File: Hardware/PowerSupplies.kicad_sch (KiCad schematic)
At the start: 56 parts, among them J3 Molex 26013114, J4 Molex 26013114, J5 Molex 26013114, J6 Molex 26013114, P1 XT60PW-M, U1 LM3414, U2 SY8303, U3 LM3414, U4 SY8303, U5 LM3414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

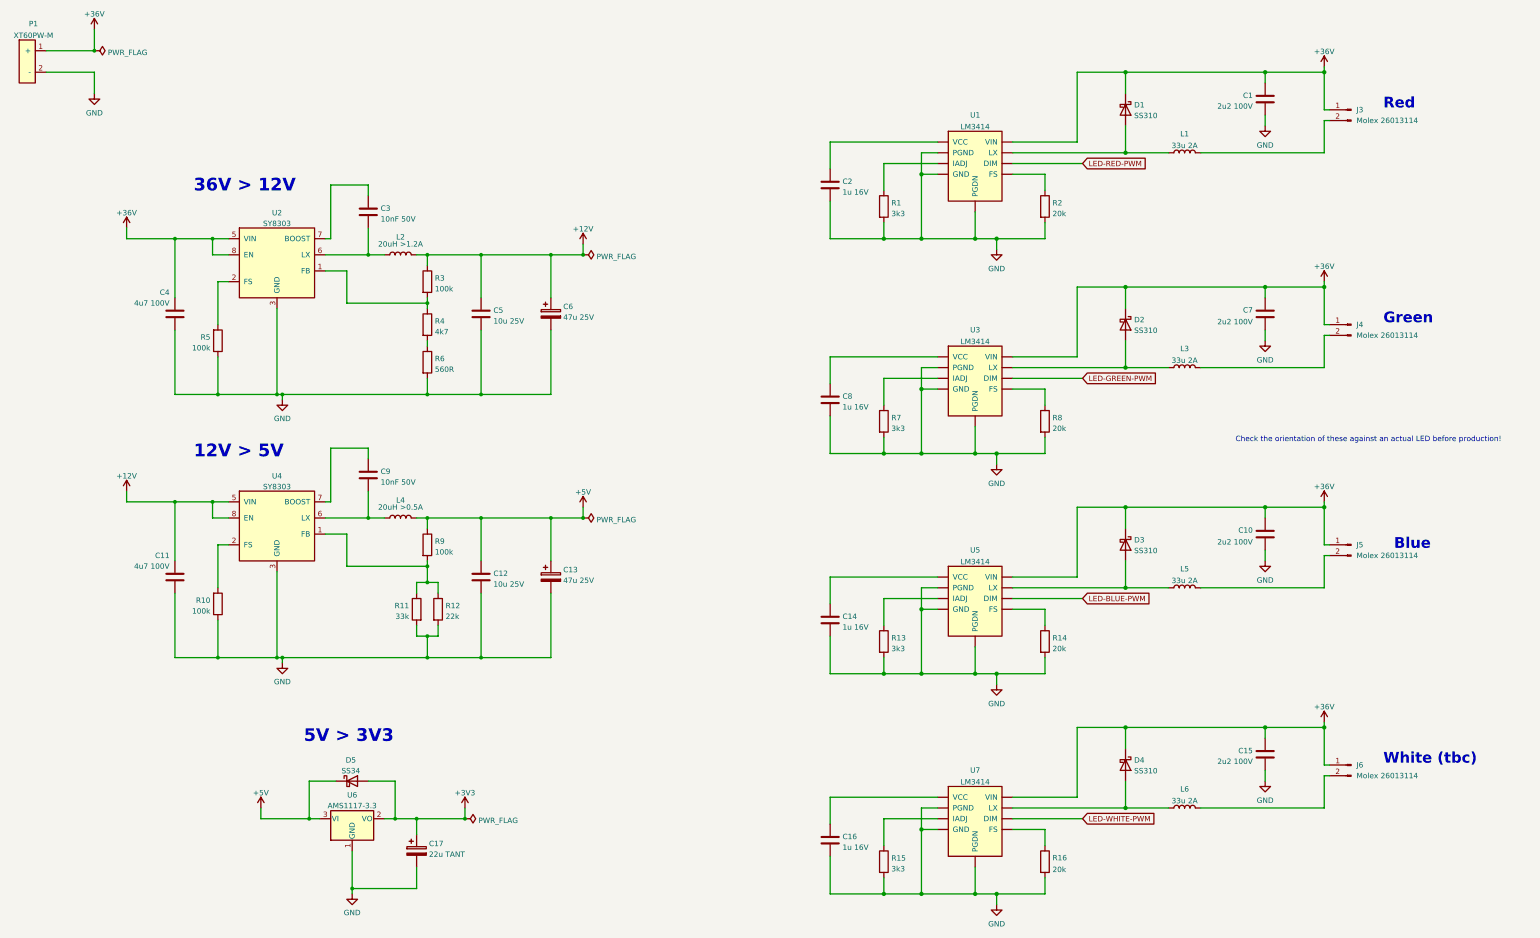
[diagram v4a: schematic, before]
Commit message: removing white channel -- limited space on side of board from inductors
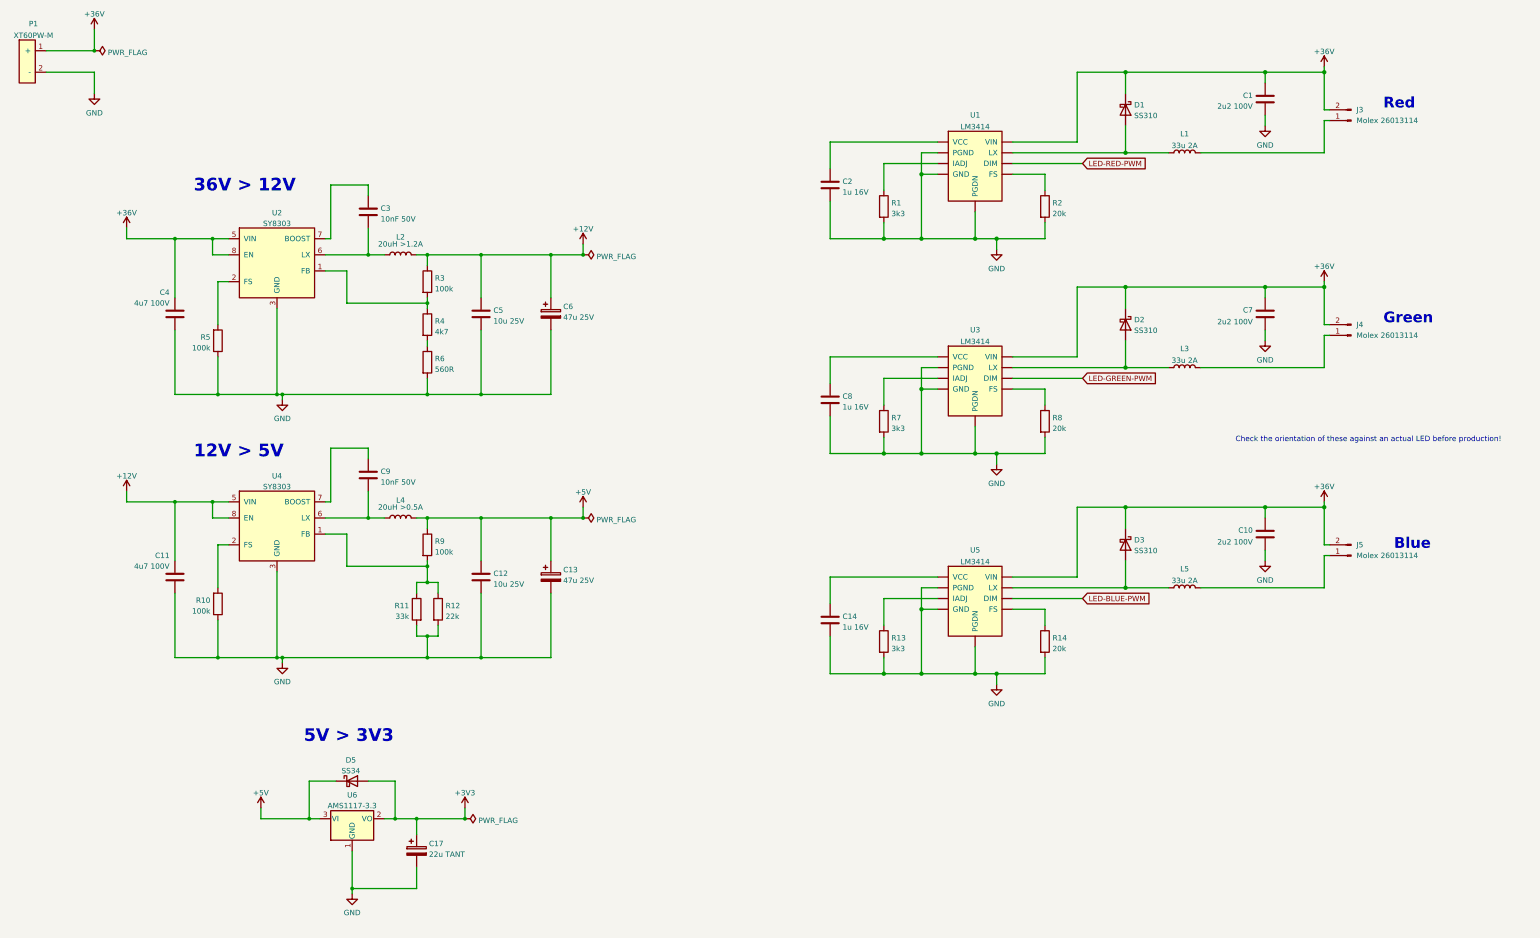
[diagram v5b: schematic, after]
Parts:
- removed C15: 2u2 100V, Capacitor_SMD:CP_Elec_6.3x5.4, symbol Device:C
- removed C16: 1u 16V, Capacitor_SMD:C_0805_2012Metric_Pad1.18x1.45mm_HandSolder, symbol Device:C
- removed D4: SS310, Diode_SMD:D_SMA_Handsoldering, symbol Device:D_Schottky
- removed J6: Molex 26013114, Connector_Molex:Molex_Mini-Fit_Jr_5569-02A2_2x01_P4.20mm_Horizontal, symbol Connector:Conn_01x02_Male
- removed L6: 33u 2A, Inductor_SMD:L_SigTra_SC3316F, symbol Device:L
- removed R15: 3k3, Resistor_SMD:R_0603_1608Metric_Pad0.98x0.95mm_HandSolder, symbol Device:R
- removed R16: 20k, Resistor_SMD:R_0603_1608Metric_Pad0.98x0.95mm_HandSolder, symbol Device:R
- removed U7: LM3414, PersonalDiscretes:TI_SO-PowerPAD-8_HandSolder, symbol PersonalDiscretes:LM3414
- L1, L3, L5: footprint Inductor_SMD:L_SigTra_SC3316F -> Inductor_SMD:L_12x12mm_H6mm; Part_number P0751.333NLT -> SMDRI127-330MT
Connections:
- net +36V: now also J3.2 (Pin_2), J4.2 (Pin_2), J5.2 (Pin_2); no longer J3.1 (Pin_1), J4.1 (Pin_1), J5.1 (Pin_1)
- net at L3.2: now also J4.1 (Pin_1); no longer J4.2 (Pin_2)
- net at L5.2: now also J5.1 (Pin_1); no longer J5.2 (Pin_2)
- net at L1.2: now also J3.1 (Pin_1); no longer J3.2 (Pin_2)
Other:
- note removed: "White (tbc)"
- moved on the sheet: J3, J4, J5

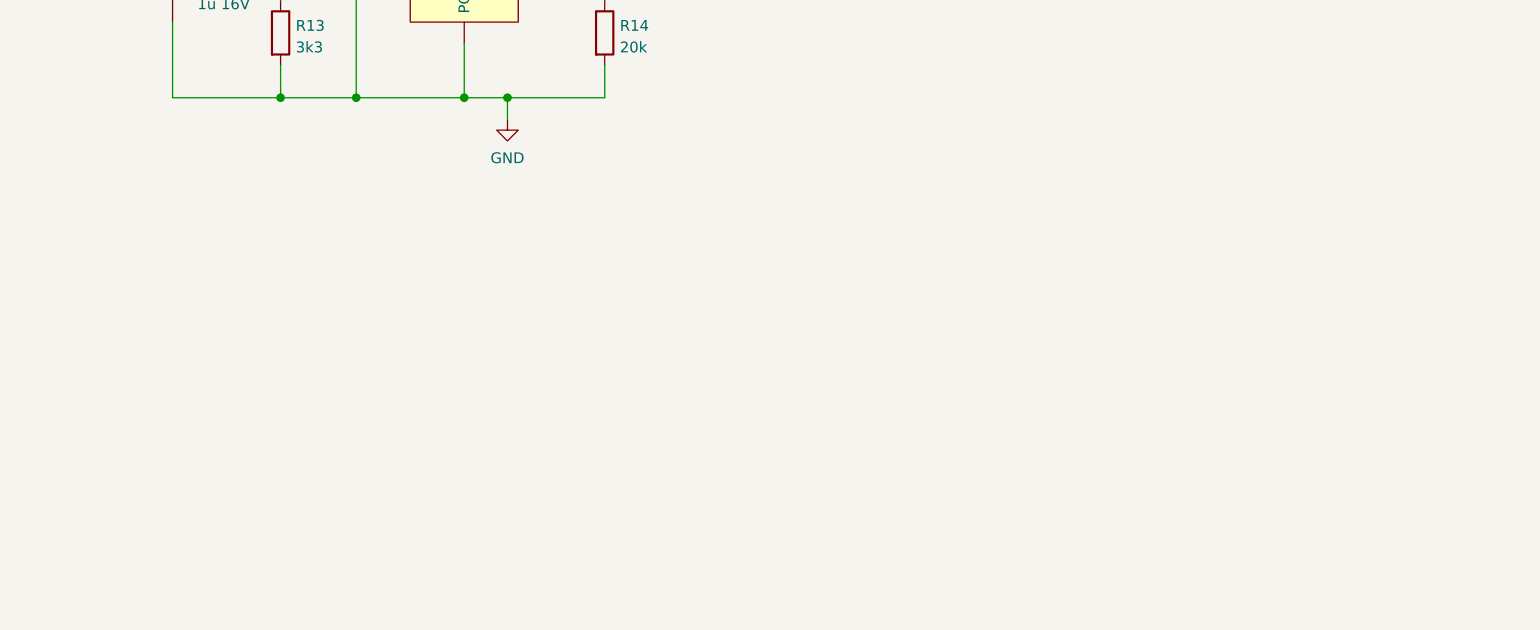
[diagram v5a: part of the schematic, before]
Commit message: white channel re-added to schem after full placement
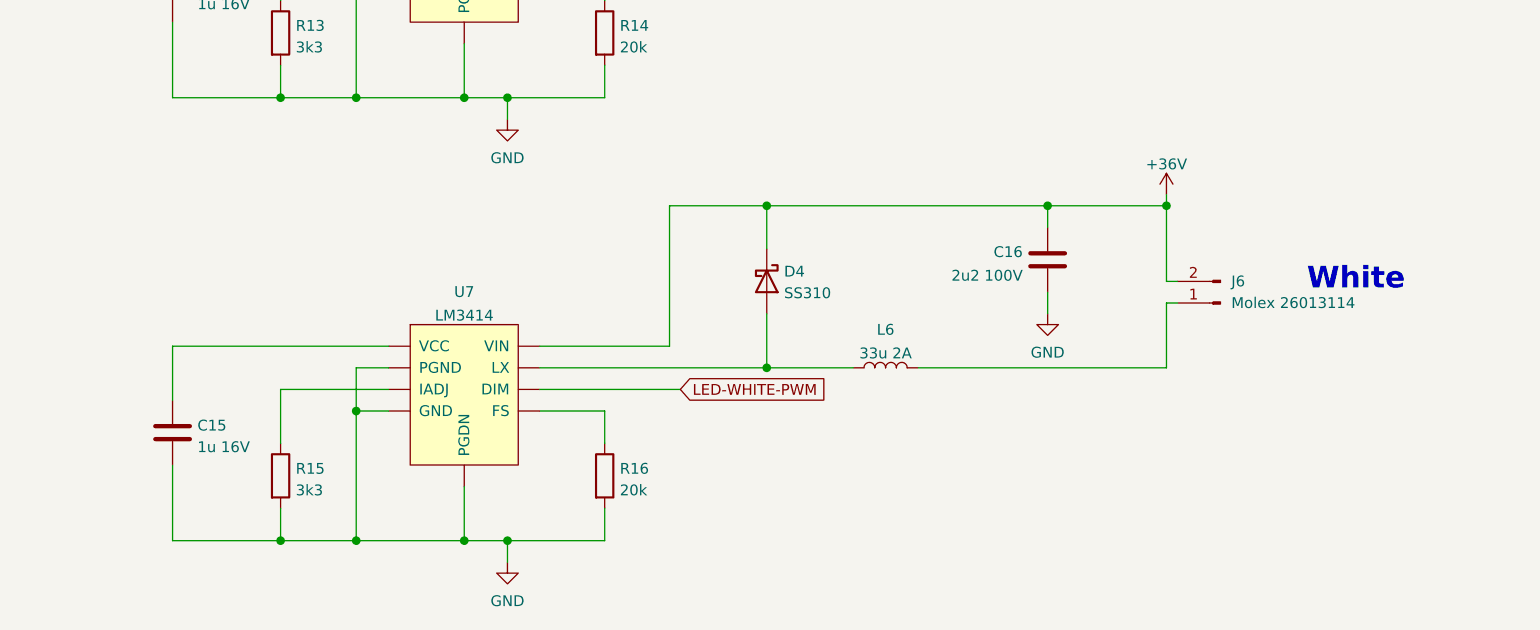
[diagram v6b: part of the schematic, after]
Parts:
- added C15: 1u 16V, Capacitor_SMD:C_0805_2012Metric_Pad1.18x1.45mm_HandSolder, symbol Device:C
- added C16: 2u2 100V, Capacitor_SMD:CP_Elec_6.3x5.4, symbol Device:C
- added D4: SS310, Diode_SMD:D_SMA_Handsoldering, symbol Device:D_Schottky
- added J6: Molex 26013114, Connector_Molex:Molex_Mini-Fit_Jr_5569-02A2_2x01_P4.20mm_Horizontal, symbol Connector:Conn_01x02_Male
- added L6: 33u 2A, Inductor_SMD:L_12x12mm_H6mm, symbol Device:L
- added R15: 3k3, Resistor_SMD:R_0603_1608Metric_Pad0.98x0.95mm_HandSolder, symbol Device:R
- added R16: 20k, Resistor_SMD:R_0603_1608Metric_Pad0.98x0.95mm_HandSolder, symbol Device:R
- added U7: LM3414, PersonalDiscretes:TI_SO-PowerPAD-8_HandSolder, symbol PersonalDiscretes:LM3414
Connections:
- net +36V: now also C16.2, D4.1 (K), J6.2 (Pin_2), U7.8 (VIN)
- net GND: now also C15.2, C16.1, R15.2, R16.2, U7.2 (PGND), U7.4 (GND), U7.9 (PGDN)
- new net: D4.2 (A), L6.1, U7.7 (LX)
- new net: J6.1 (Pin_1), L6.2
- new net: C15.1, U7.1 (VCC)
- new net: R15.1, U7.3 (IADJ)
- new net: R16.1, U7.5 (FS)
- new net LED-WHITE-PWM: U7.6 (DIM)
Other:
- note added: "White"

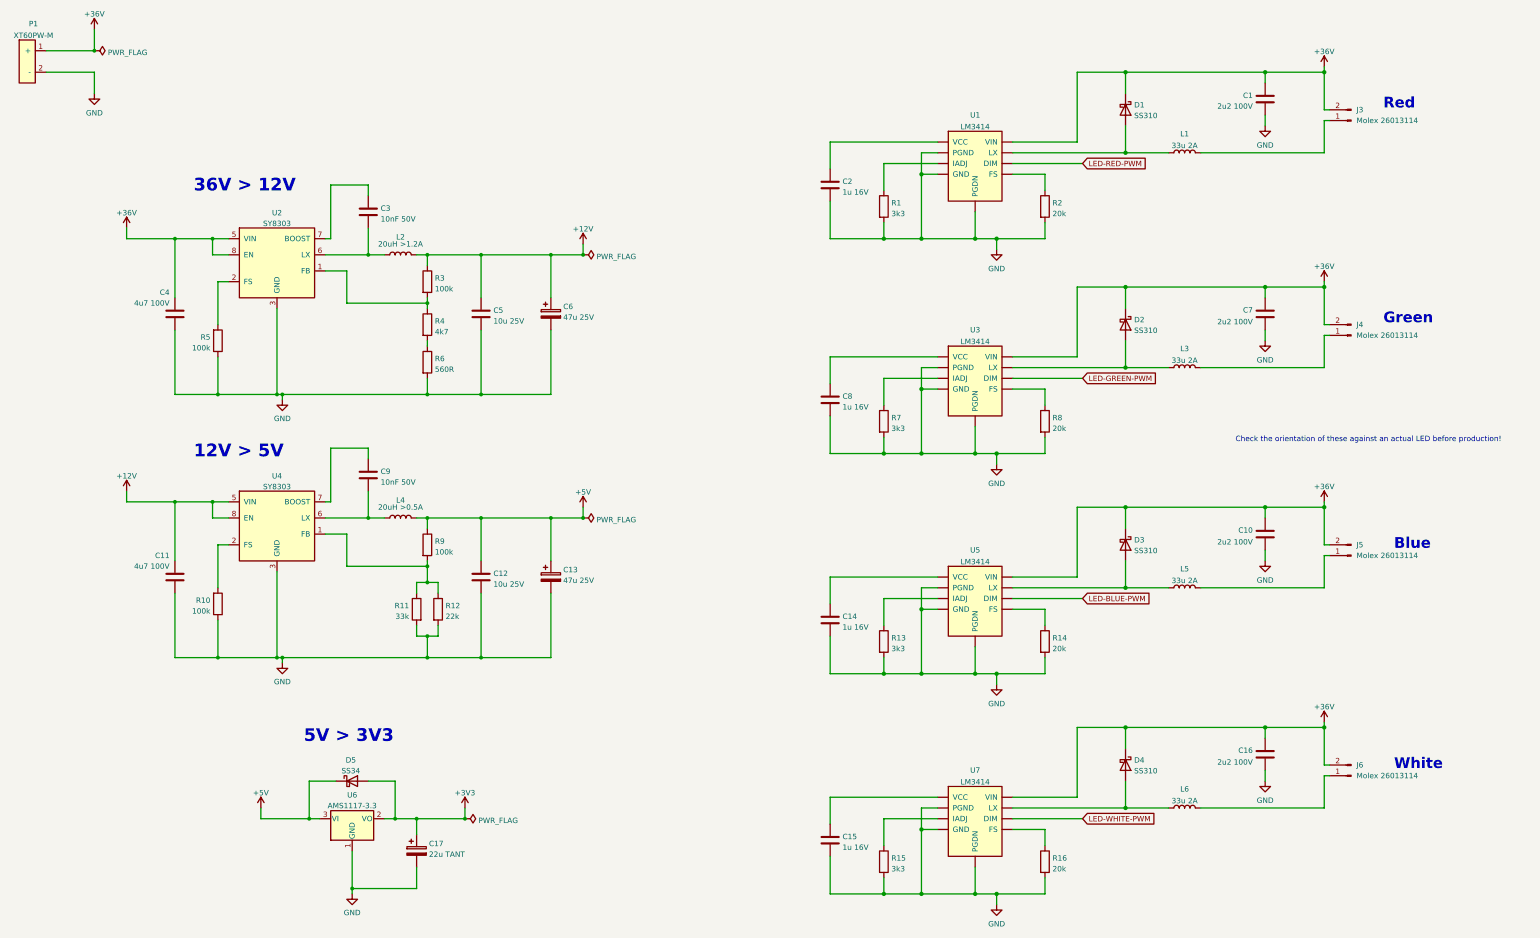
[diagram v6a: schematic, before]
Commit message: updated to new KiCAD format
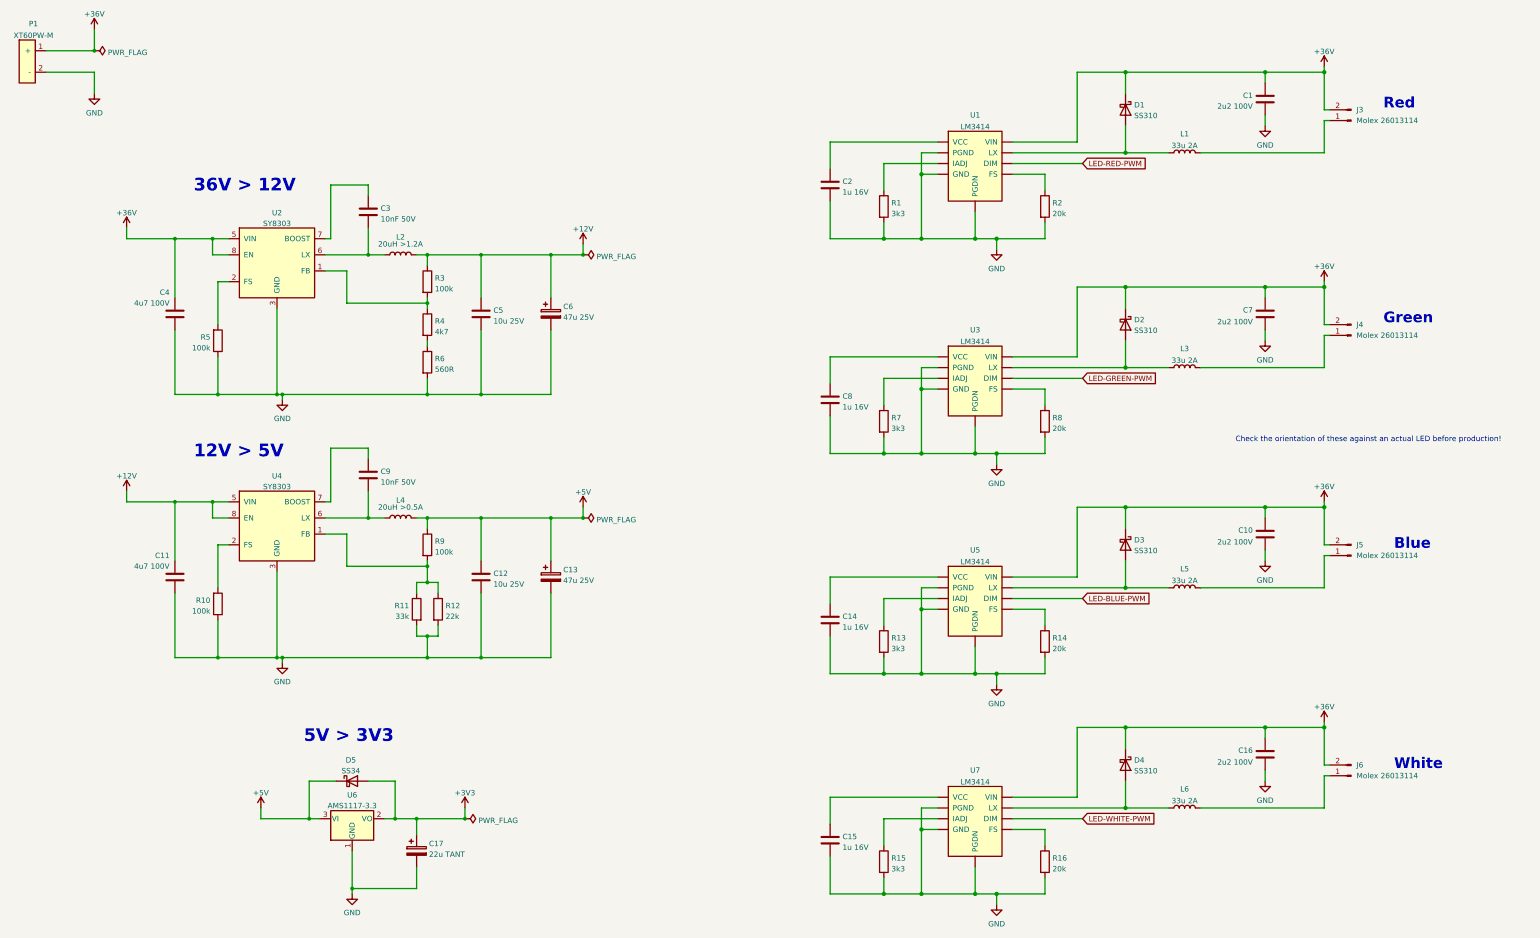
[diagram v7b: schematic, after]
